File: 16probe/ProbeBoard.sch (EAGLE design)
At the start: 60 parts, among them Q1 2N7002, Q2 2N7002, U1 LTC2495CUHFPBF, U3 MAX6037AAUKADJ+T, U4 CSTCE16M0V53A-R0, U5 TPS79733DCKR, U6 ATMEGA328P_TQFPQFN_32

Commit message: begin 16 probe layout
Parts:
- added R18, R21, R22, R23, R24, R25, R26, R27: 2.2k, SparkFun:RESISTOR0603-RES
- added TEMP1-5V1, TEMP10, TEMP11, TEMP12, TEMP13, TEMP14, TEMP15, TEMP16, TEMP2-5V1, TEMP3-5V1, TEMP4-5V1, TEMP5-5V1, TEMP6-5V1, TEMP7-5V1, TEMP8-5V1, TEMP9: (no value), wirepad:1,6/0,9
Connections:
- new net CH10: R22.1, TEMP11.P, U1.CH10
- new net CH11: R23.1, TEMP12.P, U1.CH11
- new net CH12: R24.1, TEMP13.P, U1.CH12
- new net CH13: R25.1, TEMP14.P, U1.CH13
- new net CH14: R26.1, TEMP15.P, U1.CH14
- new net CH15: R27.1, TEMP16.P, U1.CH15
- new net CH8: R18.1, TEMP9.P
- new net CH9: R21.1, TEMP10.P, U1.CH9
- net +5V: now also TEMP1-5V1.P, TEMP2-5V1.P, TEMP3-5V1.P, TEMP4-5V1.P, TEMP5-5V1.P, TEMP6-5V1.P, TEMP7-5V1.P, TEMP8-5V1.P
- net COM: now also R18.2, R21.2, R22.2, R23.2, R24.2, R25.2, R26.2, R27.2

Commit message: signal traces for 16 probe board
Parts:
- removed R27: 2.2k, SparkFun:RESISTOR0603-RES
- removed TEMP16, TEMP8-5V1: (no value), wirepad:1,6/0,9
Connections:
- removed net CH15: R27.1, TEMP16.P, U1.CH15
- net +5V: no longer TEMP8-5V1.P
- net CH10: now also U1.CH11; no longer U1.CH10
- net CH11: now also U1.CH12; no longer U1.CH11
- net CH12: now also U1.CH13; no longer U1.CH12
- net CH13: now also U1.CH14; no longer U1.CH13
- net CH14: now also U1.CH15; no longer U1.CH14
- net CH8: now also U1.CH9
- net CH9: now also U1.CH10; no longer U1.CH9
- net COM: no longer R27.2
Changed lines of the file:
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@@
 </part>
 <part name="U$60" library="MyPOW" deviceset="COM" device=""/>
-<part name="TEMP8-5V1" library="wirepad" library_urn="urn:adsk.eagle:library:412" deviceset="1,6/0,9" device="" package3d_urn="urn:adsk.eagle:package:30840/1"/>
-<part name="TEMP16" library="wirepad" library_urn="urn:adsk.eagle:library:412" deviceset="1,6/0,9" device="" package3d_urn="urn:adsk.eagle:package:30840/1"/>
-<part name="U$61" library="MyPOW" deviceset="+5V" device=""/>
-<part name="R27" library="SparkFun" deviceset="RESISTOR" device="0603-RES" value="2.2k">
-<attribute name="DIGIKEY_PART_NUMBER" value="P2.2KDBTR-ND"/>
-<attribute name="MANUFACTURER" value="Panasonic Electronic Components"/>
-<attribute name="MANUFACTURER_PART_NUMBER" value="ERA-3AEB222V"/>
-<attribute name="PRICE" value="0.03717"/>
-</part>
-<part name="U$62" library="MyPOW" deviceset="COM" device=""/>
 </parts>
 <sheets>
@@
 </segment>
 </net>
-<net name="CH9" class="0">
+<net name="CH14" class="0">
+<segment>
+<pinref part="U1" gate="A" pin="CH15"/>
+<wire x1="27.94" y1="109.22" x2="33.02" y2="109.22" width="0.1524" layer="91"/>
+<label x="33.02" y="109.22" size="1.27" layer="95" xref="yes"/>
+</segment>
+</net>
+<net name="CH8" class="0">
 <segment>
 <pinref part="U1" gate="A" pin="CH9"/>
@@
 </segment>
 </net>
-<net name="CH10" class="0">
+<net name="CH9" class="0">
 <segment>
 <pinref part="U1" gate="A" pin="CH10"/>
@@
 </segment>
 </net>
-<net name="CH11" class="0">
+<net name="CH10" class="0">
 <segment>
 <pinref part="U1" gate="A" pin="CH11"/>
@@
 </segment>
 </net>
-<net name="CH12" class="0">
+<net name="CH11" class="0">
 <segment>
 <pinref part="U1" gate="A" pin="CH12"/>
@@
 </segment>
 </net>
-<net name="CH13" class="0">
+<net name="CH12" class="0">
 <segment>
 <pinref part="U1" gate="A" pin="CH13"/>
@@
 </segment>
 </net>
-<net name="CH14" class="0">
+<net name="CH13" class="0">
 <segment>
 <pinref part="U1" gate="A" pin="CH14"/>
 <wire x1="27.94" y1="106.68" x2="33.02" y2="106.68" width="0.1524" layer="91"/>
 <label x="33.02" y="106.68" size="1.27" layer="95" xref="yes"/>
-</segment>
-</net>
-<net name="CH15" class="0">
-<segment>
-<pinref part="U1" gate="A" pin="CH15"/>
-<wire x1="27.94" y1="109.22" x2="33.02" y2="109.22" width="0.1524" layer="91"/>
-<label x="33.02" y="109.22" size="1.27" layer="95" xref="yes"/>
 </segment>
 </net>
@@
 </instance>
 <instance part="U$60" gate="G$1" x="266.7" y="-7.62" smashed="yes"/>
-<instance part="TEMP8-5V1" gate="1" x="294.64" y="22.86" smashed="yes" rot="R90">
-<attribute name="NAME" x="292.7858" y="21.717" size="1.778" layer="95" rot="R90"/>
-<attribute name="VALUE" x="297.942" y="21.717" size="1.778" layer="96" rot="R90"/>
-</instance>
-<instance part="TEMP16" gate="1" x="302.26" y="22.86" smashed="yes" rot="R270">
-<attribute name="NAME" x="304.1142" y="24.003" size="1.778" layer="95" rot="R270"/>
-<attribute name="VALUE" x="298.958" y="24.003" size="1.778" layer="96" rot="R270"/>
-</instance>
-<instance part="U$61" gate="G$1" x="294.64" y="38.1" smashed="yes">
-<attribute name="VALUE" x="292.1" y="40.64" size="1.778" layer="96"/>
-</instance>
-<instance part="R27" gate="G$1" x="302.26" y="2.54" smashed="yes" rot="R270">
-<attribute name="DIGIKEY_PART_NUMBER" x="302.26" y="2.54" size="1.778" layer="96" rot="R270" display="off"/>
-<attribute name="MANUFACTURER" x="302.26" y="2.54" size="1.778" layer="96" rot="R270" display="off"/>
-<attribute name="MANUFACTURER_PART_NUMBER" x="302.26" y="2.54" size="1.778" layer="96" rot="R270" display="off"/>
-<attribute name="PRICE" x="302.26" y="2.54" size="1.778" layer="96" rot="R270" display="off"/>
-<attribute name="NAME" x="303.7586" y="6.35" size="1.778" layer="95" rot="R270"/>
-<attribute name="VALUE" x="298.958" y="6.35" size="1.778" layer="96" rot="R270"/>
-</instance>
-<instance part="U$62" gate="G$1" x="302.26" y="-7.62" smashed="yes"/>
 </instances>
 <busses>
@@
 <wire x1="259.08" y1="35.56" x2="259.08" y2="25.4" width="0.1524" layer="91"/>
 </segment>
-<segment>
-<pinref part="U$61" gate="G$1" pin="+5V"/>
-<pinref part="TEMP8-5V1" gate="1" pin="P"/>
-<wire x1="294.64" y1="35.56" x2="294.64" y2="25.4" width="0.1524" layer="91"/>
-</segment>
 </net>
 <net name="COM" class="0">
@@
 <pinref part="R26" gate="G$1" pin="2"/>
 <wire x1="266.7" y1="-5.08" x2="266.7" y2="-2.54" width="0.1524" layer="91"/>
-</segment>
-<segment>
-<pinref part="U$62" gate="G$1" pin="COM"/>
-<pinref part="R27" gate="G$1" pin="2"/>
-<wire x1="302.26" y1="-5.08" x2="302.26" y2="-2.54" width="0.1524" layer="91"/>
 </segment>
 </net>
@@
 </segment>
 </net>
-<net name="CH15" class="0">
-<segment>
-<pinref part="TEMP16" gate="1" pin="P"/>
-<pinref part="R27" gate="G$1" pin="1"/>
-<wire x1="302.26" y1="20.32" x2="302.26" y2="12.7" width="0.1524" layer="91"/>
-<wire x1="302.26" y1="12.7" x2="302.26" y2="7.62" width="0.1524" layer="91"/>
-<wire x1="302.26" y1="12.7" x2="309.88" y2="12.7" width="0.1524" layer="91"/>
-<junction x="302.26" y="12.7"/>
-<label x="309.88" y="12.7" size="1.27" layer="95" xref="yes"/>
-</segment>
-</net>

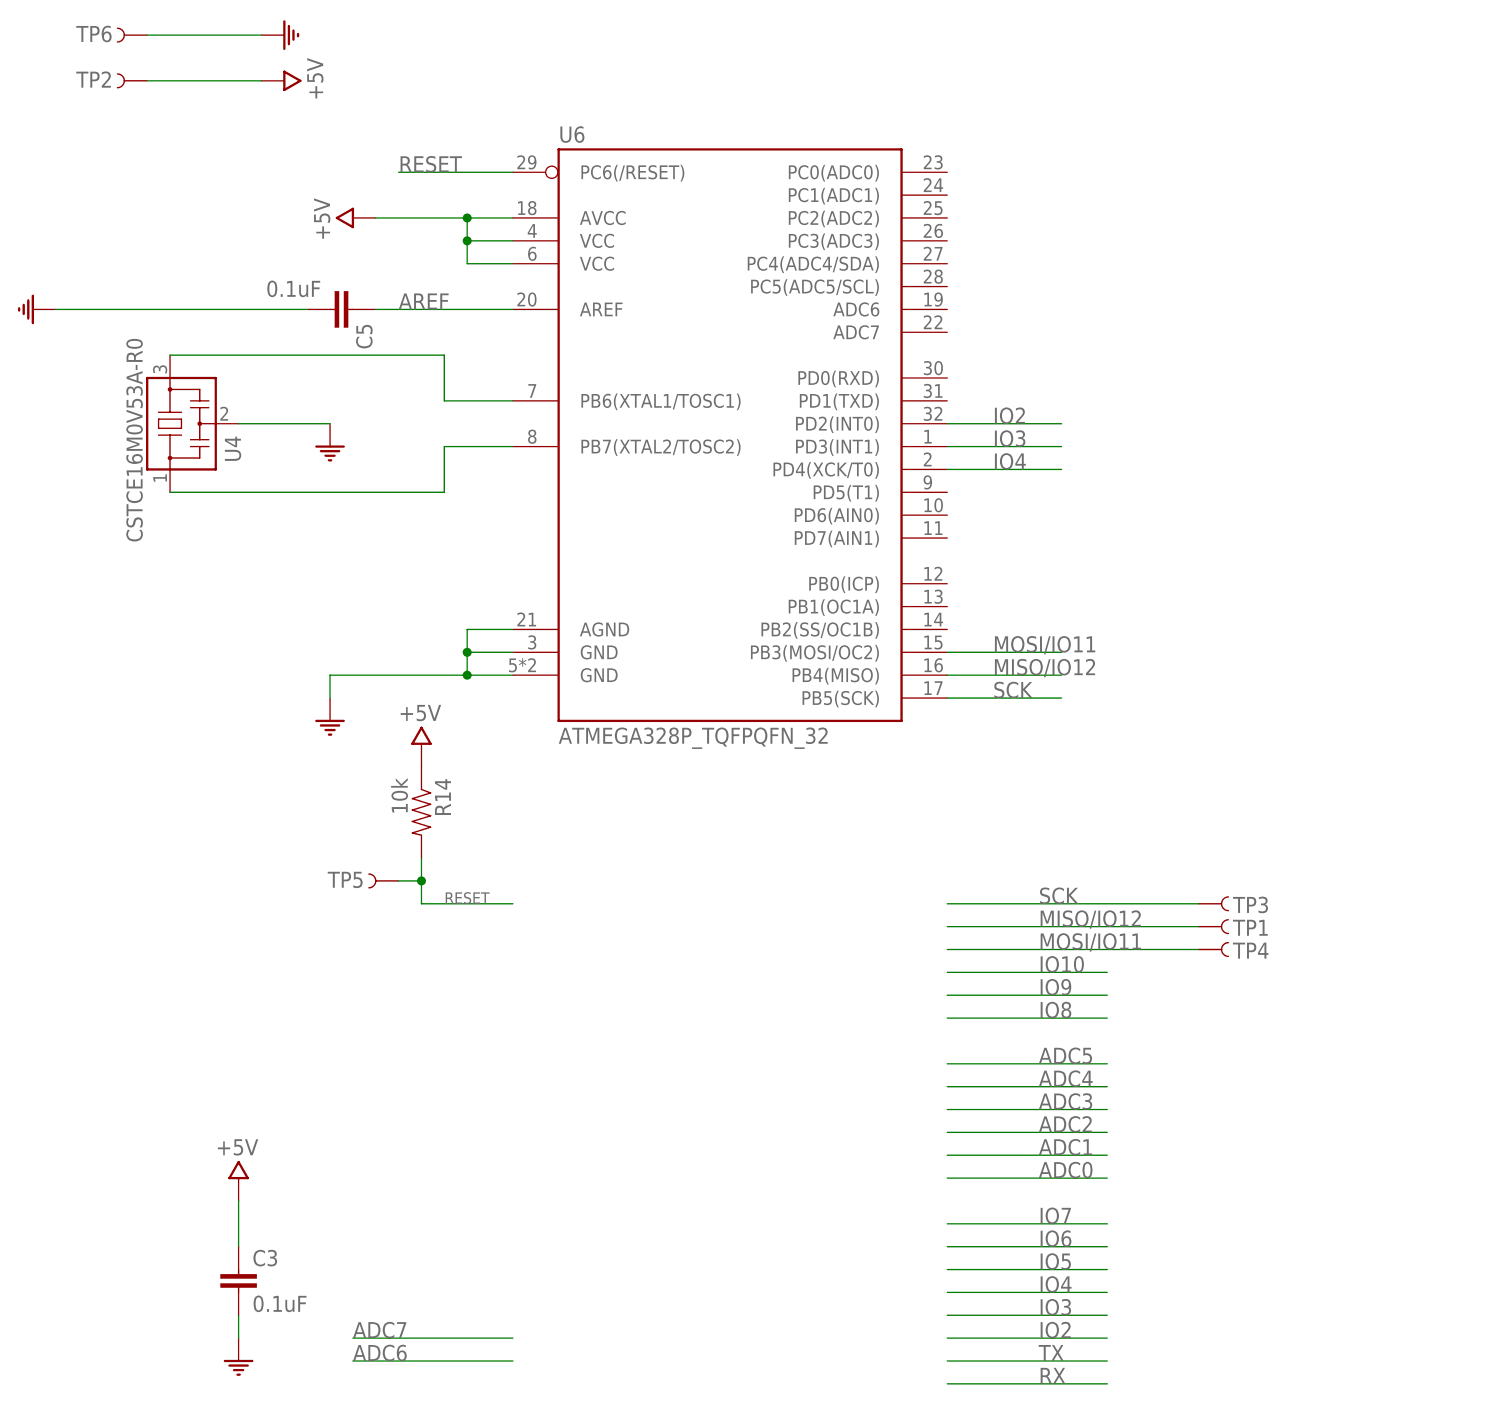
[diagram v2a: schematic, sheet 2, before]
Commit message: switch out passives and crystal
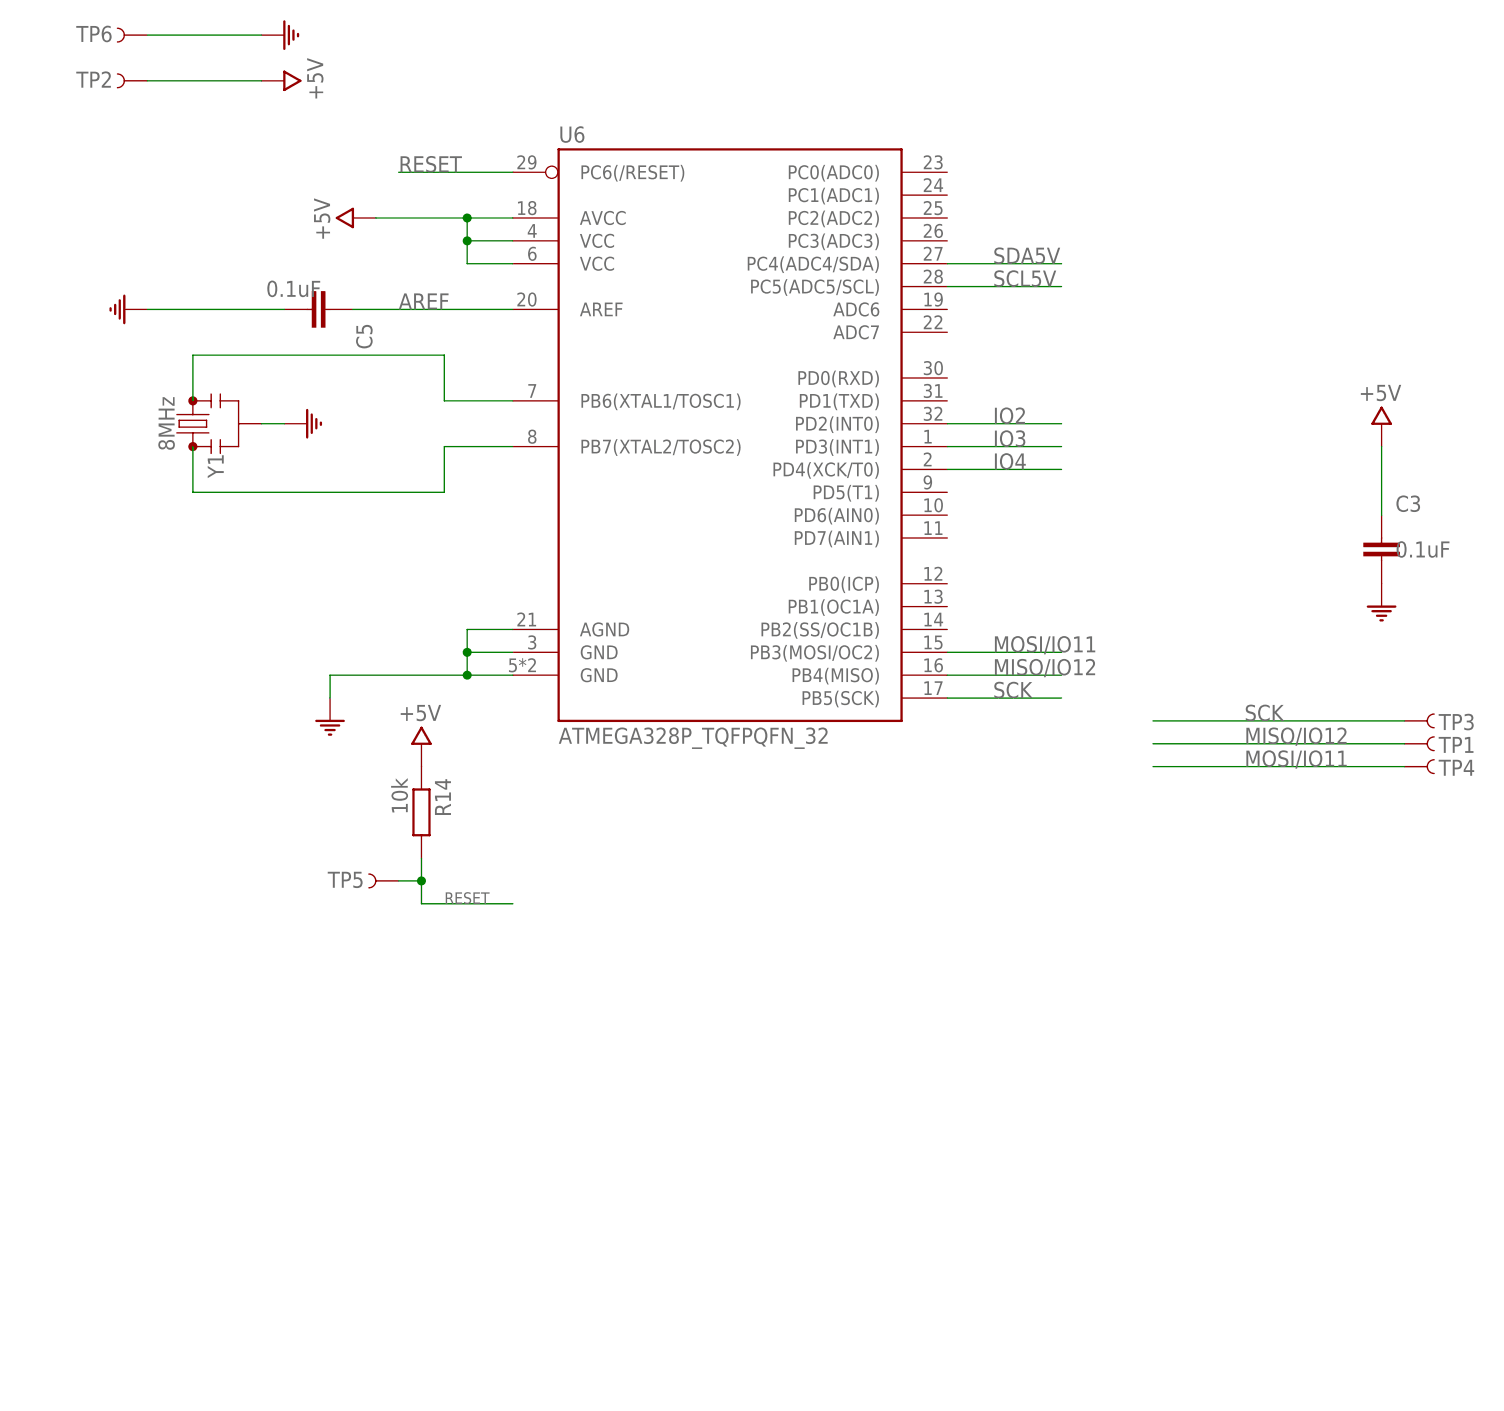
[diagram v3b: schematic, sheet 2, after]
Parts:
- removed U4: CSTCE16M0V53A-R0, Murata Resonator:CSTCE16M0V53A-R0
- added Y1: 8MHz, bschulz:RESONATOR8MHZSMD_3.2X1.3
- C1, C10, C2, C3, C5, C7, C8, C9: device SparkFun:CAP0603-CAP -> bschulz_passives:C-EUC0603
- R1, R10, R11, R12, R13, R14, R15, R16, R17, R18, R19, R2, R20, R21, R22, R23, R24, R25, R26, R3, R4, R5, R6, R7, R8, R9: device SparkFun:RESISTOR0603-RES -> bschulz_passives:R-EU_R0603
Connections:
- net COM: now also Y1.2; no longer U4.2
- net N$1: now also Y1.3; no longer U4.3
- net N$7: now also Y1.1; no longer U4.1
- net SCL5V: now also U6.PC5(ADC5/SCL)
- net SDA5V: now also U6.PC4(ADC4/SDA)
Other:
- moved on the sheet: C1, C10, C2, C3, C5, C7, C8, C9, TP1, TP3, TP4

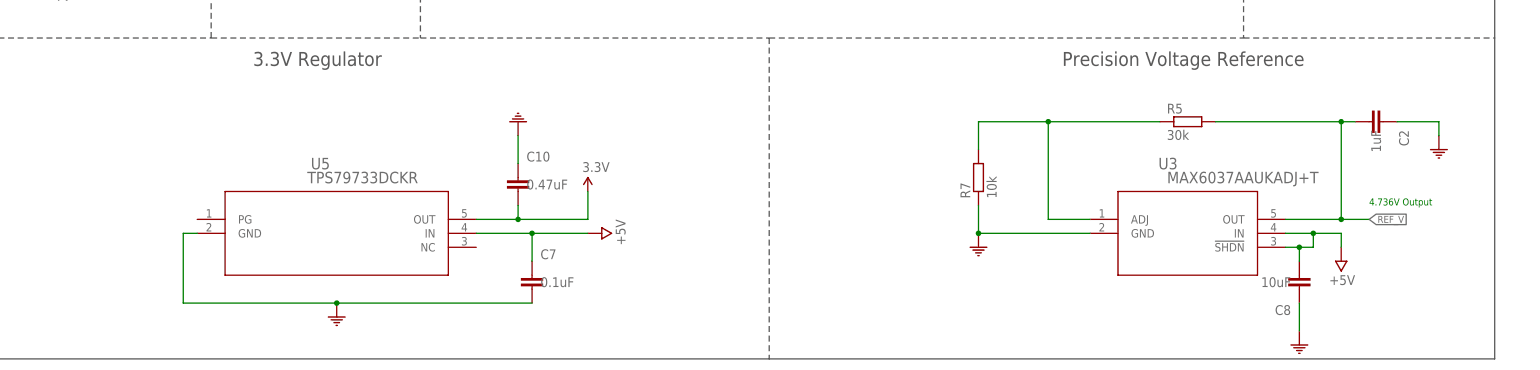
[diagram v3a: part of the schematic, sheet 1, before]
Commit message: replace voltage reference IC
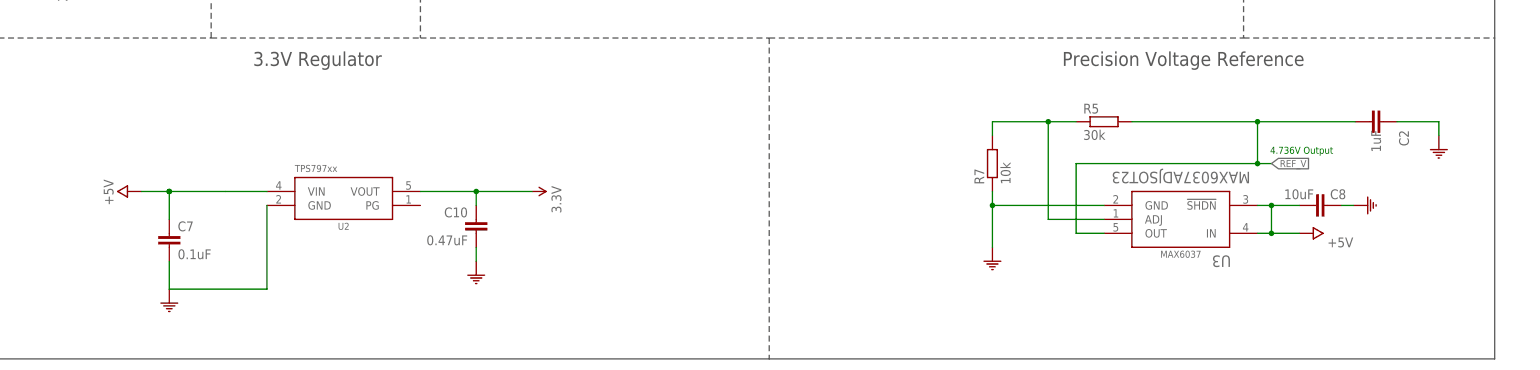
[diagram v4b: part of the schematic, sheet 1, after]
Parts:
- removed U5: TPS79733DCKR, TPS79733:TPS79733DCKR
- added U2: TPS79733, bschulz:TPS79733
- U3: value MAX6037AAUKADJ+T -> MAX6037ADJSOT23; device MAX6037AAUKADJ:MAX6037AAUKADJ+T -> bschulz:MAX6037ADJSOT23; MANUFACTURER_PART_NUMBER MAX6037AAUK33+T -> (none)
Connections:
- net +5V: now also U2.VIN; no longer U5.IN
- net 3.3V: now also U2.VOUT; no longer U5.OUT
- net COM: now also U2.GND; no longer U5.GND
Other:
- moved on the sheet: C10, C7, C8, R5, R7
